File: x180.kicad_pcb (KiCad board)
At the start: 6 copper layers, 50 x 50 mm, 77 parts, among them J1 U180 Header, J2 Conn_01x06_Pin, U1 ATF1502AS-7A, U2 ADG734, U3 ADG734, U4 ADG734, U5 ADG734

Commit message: Update of PCB
Update with pulldowns for the control lines and the option to use gate modulation. Also added CPLD code with pinkeep disabled. (Required for linearity, one needs to connect the JTAG lines to GND after programing.)
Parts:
- added C14: 100pF, Capacitor_SMD:C_0603_1608Metric, F.Cu at (95.3, 47.3)
- added R41: 5k, Resistor_SMD:R_0603_1608Metric, B.Cu at (84.8, 51.2)
- added R42: 5k, Resistor_SMD:R_0603_1608Metric, F.Cu at (72.9, 61.8)
- added R43: 5k, Resistor_SMD:R_0603_1608Metric, B.Cu at (86.5, 53.6)
- added R44: 5k, Resistor_SMD:R_0603_1608Metric, F.Cu at (72.9, 60.3)
- added R45: 5k, Resistor_SMD:R_0603_1608Metric, B.Cu at (64.1, 48.9)
- added R46: 5k, Resistor_SMD:R_0603_1608Metric, B.Cu at (52.8, 49.2)
- added R47: 5k, Resistor_SMD:R_0603_1608Metric, B.Cu at (51.7, 61.8)
- added R48: 5k, Resistor_SMD:R_0603_1608Metric, B.Cu at (61.7, 59.1)
- added R49: 5k, Resistor_SMD:R_0603_1608Metric, B.Cu at (53.4, 56.5)
- added R50: 5k, Resistor_SMD:R_0603_1608Metric, B.Cu at (61.8, 56.5)
- added R51: 5k, Resistor_SMD:R_0603_1608Metric, B.Cu at (62.7, 67.9)
- added R52: 5k, Resistor_SMD:R_0603_1608Metric, B.Cu at (54.0, 65.7)
- added R53: 5k, Resistor_SMD:R_0603_1608Metric, B.Cu at (71.6, 55.0)
- added R54: 10k, Resistor_SMD:R_0603_1608Metric, F.Cu at (93.8, 47.3)
- added R55: 0R, Resistor_SMD:R_0603_1608Metric, F.Cu at (92.2, 49.7)
- added R56: 0R, Resistor_SMD:R_0603_1608Metric, F.Cu at (92.3, 47.3)
- moved REF** 1.27 mm to (65.9, 83.0)
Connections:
- J1 pad 28: unconnected-(J1-MOD_IN1-Pad28) -> MOD_IN
- J1 pad 29: unconnected-(J1-MOD_IN2-Pad29) -> MOD_IN
- J1 pad 30: GND -> MOD_SENS
- U4 pad 18: GND -> MOD_SENS
- U4 pad 20: GND -> Net-(U4D-IN4)
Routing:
- net MOD_SENS: track 0.00 -> 25.4 mm
- net Net-(U4D-IN4): track 0.00 -> 22.5 mm
- net MOD_IN: track 0.00 -> 15.2 mm
- net S0 RUSN3: track 1.65 -> 5.12 mm
- net S6 -12ref1 20k: track 20.8 -> 23.4 mm
- net S10 +12ref1 20k: track 13.3 -> 15.9 mm
- net S8 +12ref2 20k: track 24.2 -> 26.6 mm
- net GND: track 65.9 -> 64.0 mm, vias 188 -> 205
- net S2 RUSN1: track 1.70 -> 3.50 mm
- net S11 +12ref1 80k: track 28.5 -> 30.1 mm
- net S5 -12ref2 80k: track 22.4 -> 23.7 mm
- net S7 -12ref1 80k: track 12.9 -> 14.2 mm
- net S3 LADSN: track 2.84 -> 4.05 mm
- net S4 -12ref2 20k: track 15.6 -> 16.8 mm
- net S1 RUSN2: track 2.84 -> 4.04 mm
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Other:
- board size 50 x 50 mm -> 50 x 51 mm
- board text added: "REV A 2 x180"
- board text added: "Simon B. 12/2025"
- board text removed: "REV A x180"

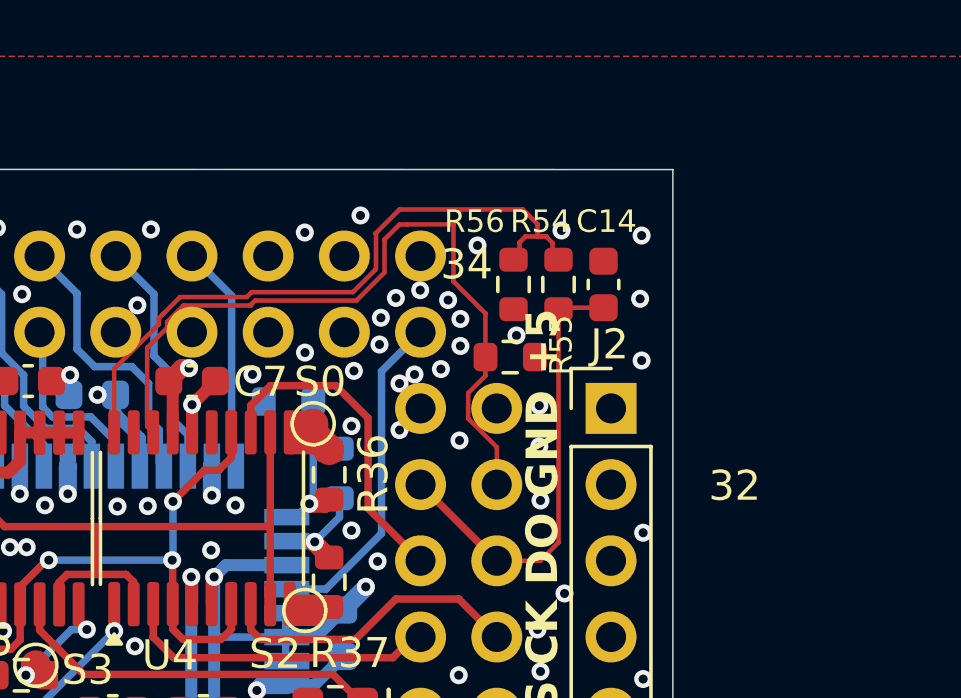
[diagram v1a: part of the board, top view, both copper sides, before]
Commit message: Fixed the gate voltage modulation
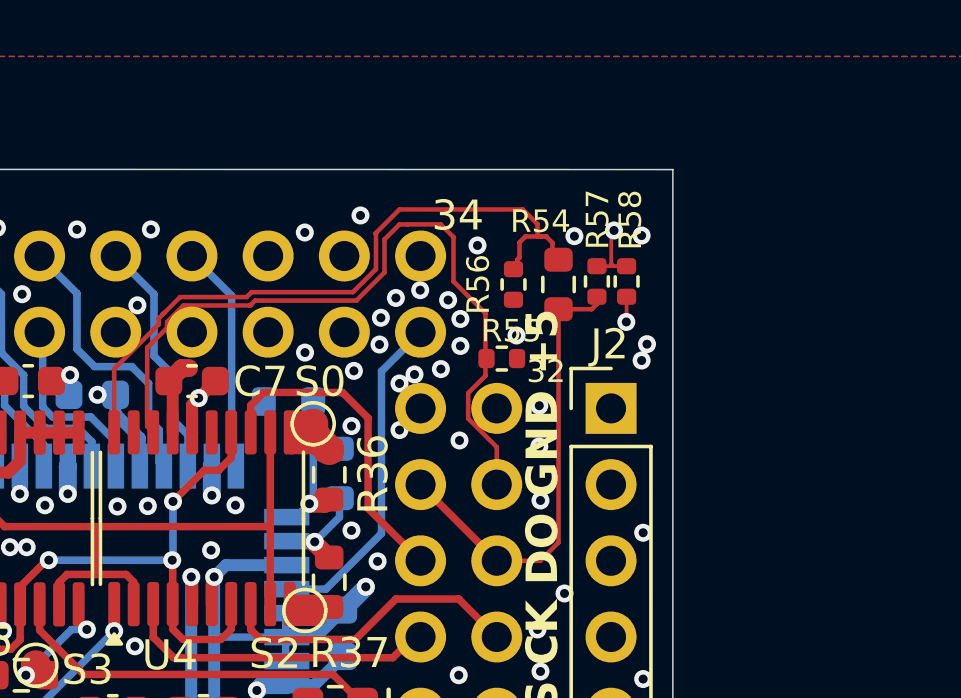
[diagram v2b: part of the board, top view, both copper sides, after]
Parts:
- removed C14: 100pF, Capacitor_SMD:C_0603_1608Metric
- added R57: 0R, Resistor_SMD:R_0402_1005Metric, F.Cu at (95.1, 47.2)
- added R58: 0R, Resistor_SMD:R_0402_1005Metric, F.Cu at (96.1, 47.2)
- R55, R56: footprint Resistor_SMD:R_0603_1608Metric -> Resistor_SMD:R_0402_1005Metric
- moved R55 0.28 mm to (91.9, 49.8)
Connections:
- C7 pad 2: VDD -> Net-(U4E-VDD)
- U4 pad 16: VDD -> Net-(U4E-VDD)
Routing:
- net Net-(U4E-VDD): track 0.00 -> 22.4 mm, vias 0 -> 2
- net VDD: track 33.7 -> 32.5 mm
- net GND: vias 205 -> 203
